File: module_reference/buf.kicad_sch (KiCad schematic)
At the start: 48 parts, among them J401 Conn_01x01, Q401 MMBT3904, U401 ADA4523, U402 ADG5401F, U403 ADA4523, U404 ADA4523, U405 D60V0L4B10LP

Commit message: Rev. 1.0
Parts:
- removed R411, R415: 0R, Resistor_SMD:R_0805_2012Metric, symbol Device:R
- added C415: 470n, Capacitor_SMD:C_1206_3216Metric, symbol Device:C
- added C416, C417, C419: 100n 50V, Capacitor_SMD:C_0603_1608Metric, symbol Device:C
- added C418: 22u 25V, Capacitor_SMD:C_1206_3216Metric, symbol Device:C
- added C420, C421: 1u, Capacitor_SMD:C_0805_2012Metric, symbol Device:C
- added JP410, JP411: Jumper_2_Bridged, Jumper:SolderJumper-2_P1.3mm_Bridged_RoundedPad1.0x1.5mm, symbol Jumper:Jumper_2_Bridged
- added RN402: DNP, Crystal:Resonator-3Pin_W10.0mm_H5.0mm, symbol Device:VoltageDivider
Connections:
- net ADR_Pin7: now also C415.2, RN402.3
- net GNDf: now also C418.2, C420.2, C421.2
- net JP404_pin2: now also C418.1, RN402.1
- net OutHf: now also C421.1
- net OutLf: now also C420.1
- net U401_+in: now also C415.1
- net U401_-in: now also C416.2, RN402.2
- net U401_out: now also C416.1
- net U402_D: now also JP410.2 (B)
- net U402_DFB: now also JP411.2 (B)
- net U403_-in: now also C417.2
- net U403_out: now also C417.1
- net U404_-in: now also C419.2, JP411.1 (A)
- net U404_out: now also C419.1, JP410.1 (A)
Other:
- moved on the sheet: C404

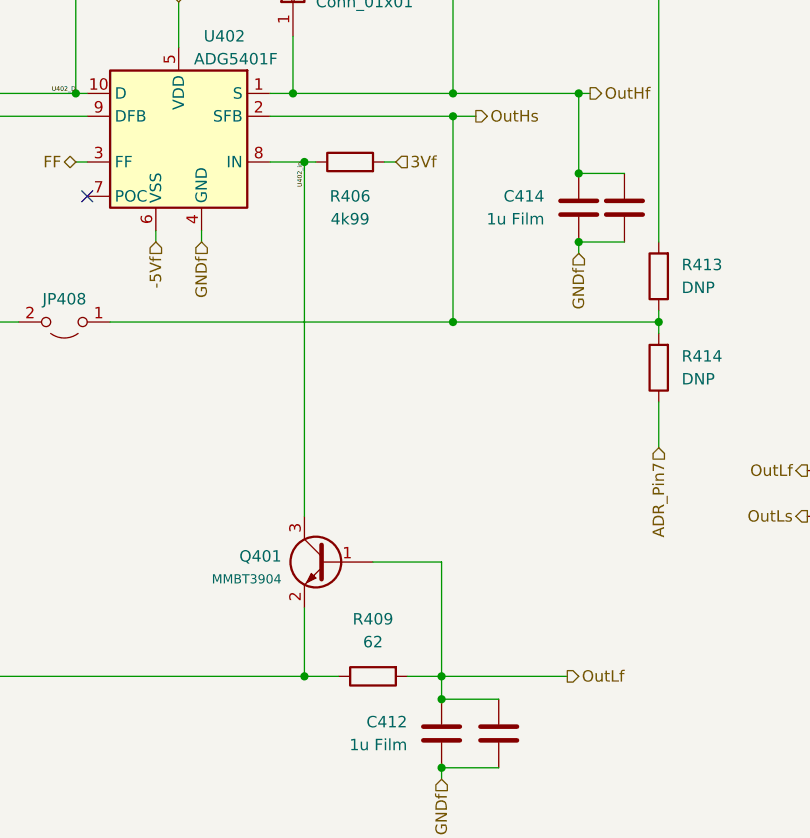
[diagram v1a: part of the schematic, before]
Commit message: corrected noise measurements
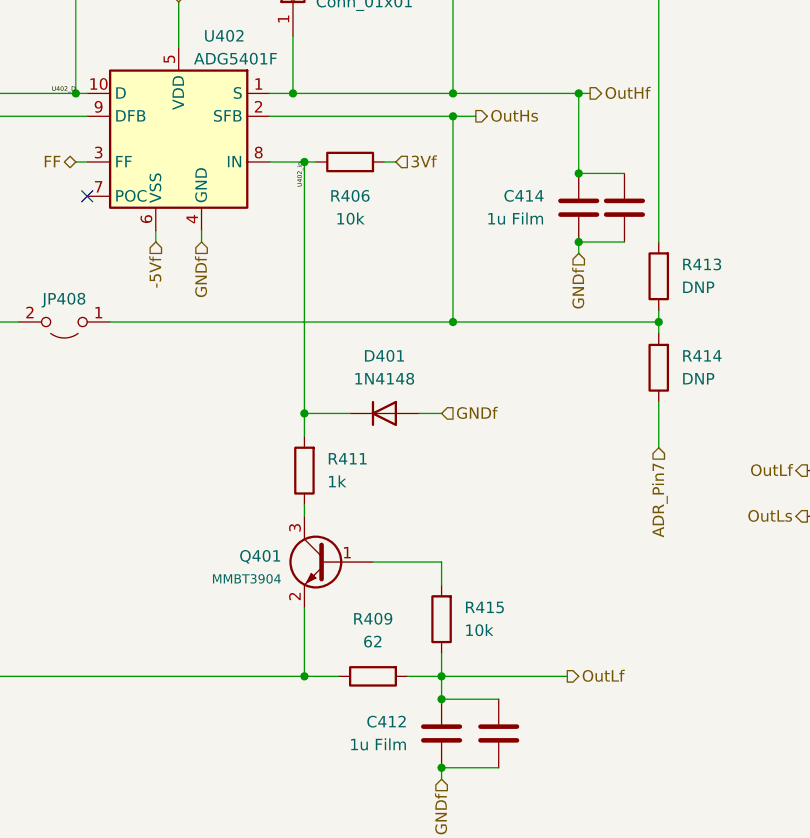
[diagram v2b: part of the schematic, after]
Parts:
- added D401: 1N4148, Diode_SMD:D_SOD-123, symbol Device:D
- added R411: 1k, Resistor_SMD:R_0805_2012Metric, symbol Device:R
- added R415: 10k, Resistor_SMD:R_0805_2012Metric, symbol Device:R
- R406: value 4k99 -> 10k
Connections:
- net GNDf: now also D401.2 (A)
- net OutLf: now also R415.1; no longer Q401.1 (B)
- net U402_in: now also D401.1 (K), R411.2; no longer Q401.3 (C)
- new net: Q401.1 (B), R415.2
- new net: Q401.3 (C), R411.1
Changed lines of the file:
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@@
   (junction (at 73.66 161.29) (diameter 0) (color 0 0 0 0)
   )
+  (junction (at 193.04 66.04) (diameter 0) (color 0 0 0 0)
+  )
   (junction (at 129.54 173.99) (diameter 0) (color 0 0 0 0)
   )
@@
   (junction (at 60.96 107.95) (diameter 0) (color 0 0 0 0)
   )
+  (junction (at 193.04 93.98) (diameter 0) (color 0 0 0 0)
+  )
   (junction (at 223.52 67.31) (diameter 0) (color 0 0 0 0)
   )
@@
   )
   (junction (at 209.55 60.96) (diameter 0) (color 0 0 0 0)
-  )
-  (junction (at 193.04 66.04) (diameter 0) (color 0 0 0 0)
   )
   (junction (at 123.19 64.77) (diameter 0) (color 0 0 0 0)
@@
     (stroke (width 0) (type default) (color 0 0 0 0))
   )
+  (wire (pts (xy 198.12 93.98) (xy 193.04 93.98))
+    (stroke (width 0) (type default) (color 0 0 0 0))
+  )
   (wire (pts (xy 59.69 161.29) (xy 64.77 161.29))
     (stroke (width 0) (type default) (color 0 0 0 0))
@@
     (stroke (width 0) (type default) (color 0 0 0 0))
   )
+  (wire (pts (xy 193.04 93.98) (xy 193.04 66.04))
+    (stroke (width 0) (type default) (color 0 0 0 0))
+  )
   (wire (pts (xy 69.85 27.94) (xy 69.85 30.48))
     (stroke (width 0) (type default) (color 0 0 0 0))
@@
     (stroke (width 0) (type default) (color 0 0 0 0))
   )
+  (wire (pts (xy 193.04 96.52) (xy 193.04 93.98))
+    (stroke (width 0) (type default) (color 0 0 0 0))
+  )
   (wire (pts (xy 78.74 138.43) (xy 82.55 138.43))
     (stroke (width 0) (type default) (color 0 0 0 0))
@@
     (stroke (width 0) (type default) (color 0 0 0 0))
   )
+  (wire (pts (xy 208.28 113.03) (xy 208.28 110.49))
+    (stroke (width 0) (type default) (color 0 0 0 0))
+  )
   (wire (pts (xy 35.56 49.53) (xy 35.56 53.34))
     (stroke (width 0) (type default) (color 0 0 0 0))
@@
     (stroke (width 0) (type default) (color 0 0 0 0))
   )
+  (wire (pts (xy 208.28 120.65) (xy 208.28 123.19))
+    (stroke (width 0) (type default) (color 0 0 0 0))
+  )
   (wire (pts (xy 134.62 77.47) (xy 137.16 77.47))
     (stroke (width 0) (type default) (color 0 0 0 0))
@@
     (stroke (width 0) (type default) (color 0 0 0 0))
   )
+  (wire (pts (xy 193.04 66.04) (xy 194.31 66.04))
+    (stroke (width 0) (type default) (color 0 0 0 0))
+  )
   (wire (pts (xy 80.01 81.28) (xy 80.01 83.82))
     (stroke (width 0) (type default) (color 0 0 0 0))
@@
     (stroke (width 0) (type default) (color 0 0 0 0))
   )
-  (wire (pts (xy 193.04 66.04) (xy 193.04 105.41))
-    (stroke (width 0) (type default) (color 0 0 0 0))
-  )
   (wire (pts (xy 54.61 189.23) (xy 59.69 189.23))
     (stroke (width 0) (type default) (color 0 0 0 0))
@@
     (stroke (width 0) (type default) (color 0 0 0 0))
   )
-  (wire (pts (xy 208.28 110.49) (xy 208.28 123.19))
-    (stroke (width 0) (type default) (color 0 0 0 0))
-  )
   (wire (pts (xy 73.66 129.54) (xy 72.39 129.54))
     (stroke (width 0) (type default) (color 0 0 0 0))
@@
     (stroke (width 0) (type default) (color 0 0 0 0))
   )
+  (wire (pts (xy 193.04 105.41) (xy 193.04 104.14))
+    (stroke (width 0) (type default) (color 0 0 0 0))
+  )
   (wire (pts (xy 91.44 189.23) (xy 100.33 189.23))
     (stroke (width 0) (type default) (color 0 0 0 0))
@@
     (stroke (width 0) (type default) (color 0 0 0 0))
   )
-  (wire (pts (xy 193.04 66.04) (xy 194.31 66.04))
-    (stroke (width 0) (type default) (color 0 0 0 0))
-  )
   (wire (pts (xy 123.19 19.05) (xy 123.19 21.59))
     (stroke (width 0) (type default) (color 0 0 0 0))
@@
   )
   (wire (pts (xy 114.3 55.88) (xy 101.6 55.88))
+    (stroke (width 0) (type default) (color 0 0 0 0))
+  )
+  (wire (pts (xy 208.28 93.98) (xy 205.74 93.98))
     (stroke (width 0) (type default) (color 0 0 0 0))
   )
@@
   (label "ADR_Pin7" (at 129.54 190.5 0)
     (effects (font (size 1.27 1.27)) (justify left bottom))
+  )
+  (hierarchical_label "GNDf" (shape input) (at 208.28 93.98 0)
+    (effects (font (size 1.27 1.27)) (justify left))
   )
   (hierarchical_label "OutHf" (shape output) (at 274.32 105.41 0)
@@
     (pin "9")
   )
+  (symbol (lib_id "Device:D") (at 201.93 93.98 0) (unit 1)
+    (in_bom yes) (on_board yes) (fields_autoplaced)
+    (property "Reference" "D401" (id 0) (at 201.93 87.63 0))
+    (property "Value" "1N4148" (id 1) (at 201.93 90.17 0))
+    (property "Footprint" "Diode_SMD:D_SOD-123" (id 2) (at 201.93 93.98 0)
+      (effects (font (size 1.27 1.27)) hide)
+    )
+    (property "Datasheet" "~" (id 3) (at 201.93 93.98 0)
+      (effects (font (size 1.27 1.27)) hide)
+    )
+    (pin "1")
+    (pin "2")
+  )
   (symbol (lib_id "Device:R") (at 85.09 81.28 90) (unit 1)
     (in_bom no) (on_board yes) (fields_autoplaced)
@@
     (in_bom yes) (on_board yes) (fields_autoplaced)
     (property "Reference" "R406" (id 0) (at 198.12 69.85 90))
-    (property "Value" "4k99" (id 1) (at 198.12 72.39 90))
+    (property "Value" "10k" (id 1) (at 198.12 72.39 90))
     (property "Footprint" "Resistor_SMD:R_0805_2012Metric" (id 2) (at 198.12 67.818 90)
       (effects (font (size 1.27 1.27)) hide)
@@
     (pin "2")
   )
+  (symbol (lib_id "Device:R") (at 208.28 116.84 180) (unit 1)
+    (in_bom yes) (on_board yes) (fields_autoplaced)
+    (property "Reference" "R415" (id 0) (at 210.82 115.5699 0)
+      (effects (font (size 1.27 1.27)) (justify right))
+    )
+    (property "Value" "10k" (id 1) (at 210.82 118.1099 0)
+      (effects (font (size 1.27 1.27)) (justify right))
+    )
+    (property "Footprint" "Resistor_SMD:R_0805_2012Metric" (id 2) (at 210.058 116.84 90)
+      (effects (font (size 1.27 1.27)) hide)
+    )
+    (property "Datasheet" "~" (id 3) (at 208.28 116.84 0)
+      (effects (font (size 1.27 1.27)) hide)
+    )
+    (pin "1")
+    (pin "2")
+  )
   (symbol (lib_id "Device:C") (at 167.64 22.86 180) (unit 1)
     (in_bom yes) (on_board yes) (fields_autoplaced)
@@
     (pin "9")
   )
+  (symbol (lib_id "Device:R") (at 193.04 100.33 180) (unit 1)
+    (in_bom yes) (on_board yes) (fields_autoplaced)
+    (property "Reference" "R411" (id 0) (at 195.58 99.0599 0)
+      (effects (font (size 1.27 1.27)) (justify right))
+    )
+    (property "Value" "1k" (id 1) (at 195.58 101.5999 0)
+      (effects (font (size 1.27 1.27)) (justify right))
+    )
+    (property "Footprint" "Resistor_SMD:R_0805_2012Metric" (id 2) (at 194.818 100.33 90)
+      (effects (font (size 1.27 1.27)) hide)
+    )
+    (property "Datasheet" "~" (id 3) (at 193.04 100.33 0)
+      (effects (font (size 1.27 1.27)) hide)
+    )
+    (pin "1")
+    (pin "2")
+  )
   (symbol (lib_id "Device:R") (at 90.17 55.88 270) (unit 1)

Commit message: Rev 1.1 & Kicad 7 update
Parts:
- removed U405: D60V0L4B10LP, Package_DFN_QFN:Diodes_UDFN-10_1.0x2.5mm_P0.5mm, symbol Power_Protection:D3V3XA4B10LP
- added D402, D403: D_TVS_Dual_AAC, Package_TO_SOT_SMD:SOT-23-3, symbol Device:D_TVS_Dual_AAC
- C415: footprint Capacitor_SMD:C_1206_3216Metric -> Capacitor_SMD:C_0805_2012Metric
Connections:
- net Earth: now also D402.3 (common), D403.3 (common)
- net GNDf: now also D403.1 (A1)
- net OutHf: now also D403.2 (A2)
- net OutLf: now also D402.1 (A1)
- net OutLs: now also D402.2 (A2)
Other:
- moved on the sheet: R412, RN402

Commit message: Rev 1.2
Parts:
- removed D401: 1N4148, Diode_SMD:D_SOD-123, symbol Device:D
- added D401: 1N4148W, Diode_SMD:D_SOD-123, symbol Diode:1N4148W
- added D404: 1N4148, Diode_SMD:D_SOD-123, symbol Device:D
- added JP412: Jumper_2_Open, Jumper:SolderJumper-2_P1.3mm_Open_RoundedPad1.0x1.5mm, symbol Jumper:Jumper_2_Open
- C401, C404, C408, C409, C412, C413, C414: now left out of the parts list
- C415, C416, C417, C418, C419, C420, C421: now in the parts list
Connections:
- net GNDf: now also D401.2 (A), D404.1 (K)
- net JP406_Pin2: now also JP412.1 (A)
- net RN401_Pin9: now also JP412.2 (B)
- net U402_in: now also D401.1 (K)
- net U403_out: now also D404.2 (A)
